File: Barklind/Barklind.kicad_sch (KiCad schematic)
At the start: 4 parts, among them J1 Molex 47053-1000, J2 Molex 47053-1000, J3 Molex 47053-1000, J4 RJ45_Abracon_ARJP11A-MASA-B-A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

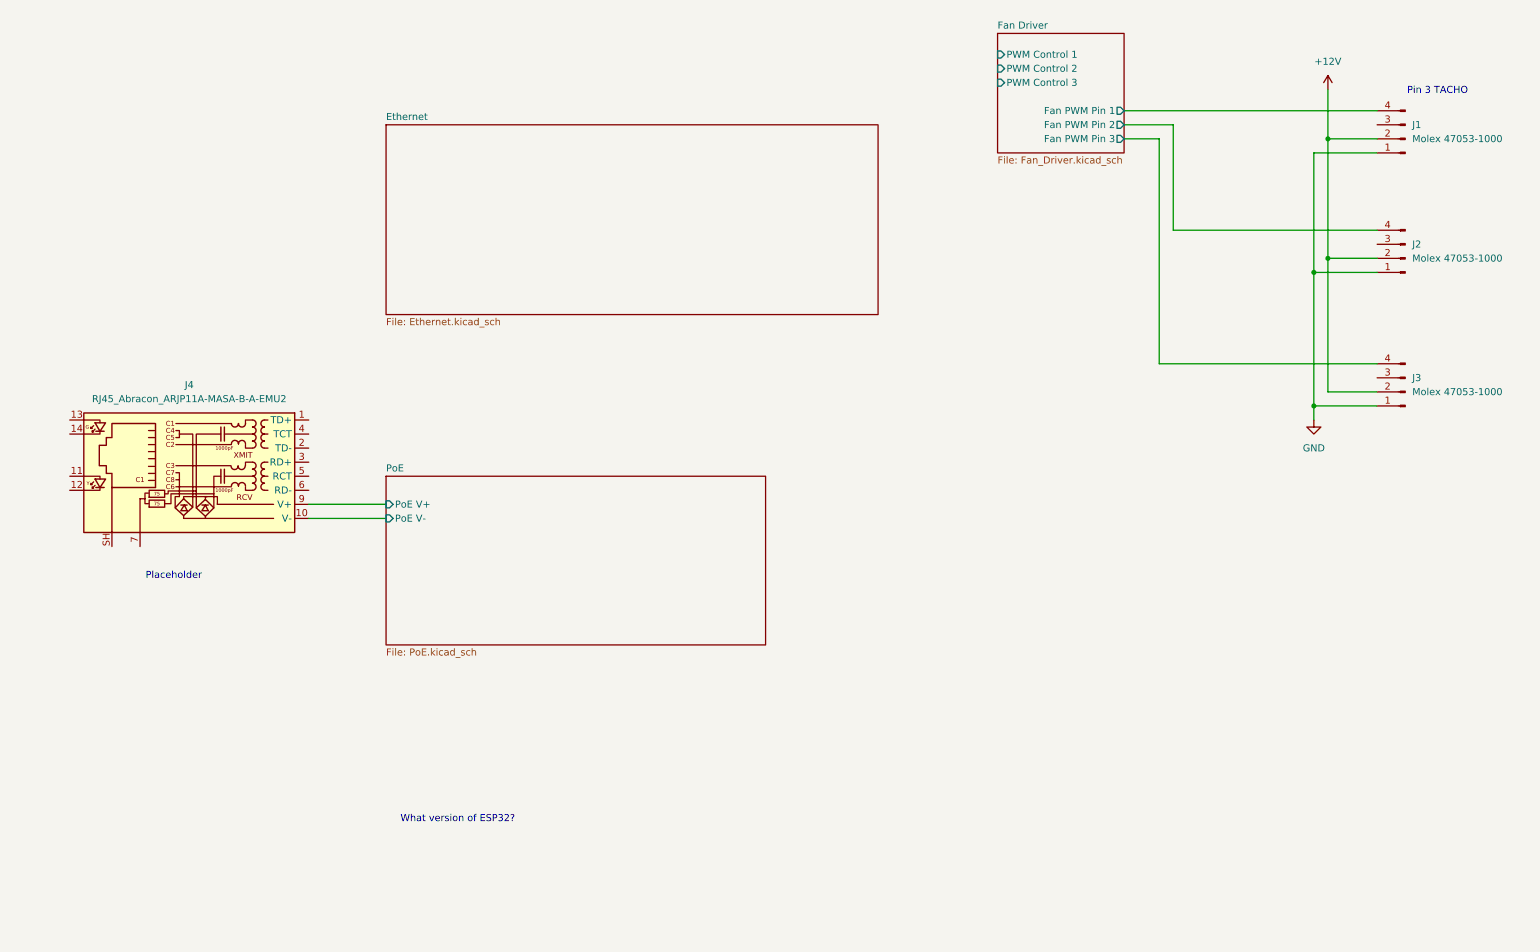
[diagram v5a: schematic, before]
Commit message: Added ESP32-DevkitC Updated workflow to commit changes (adding built docs) Removed manually exported PDF schematic in favour of auto-exported schematic
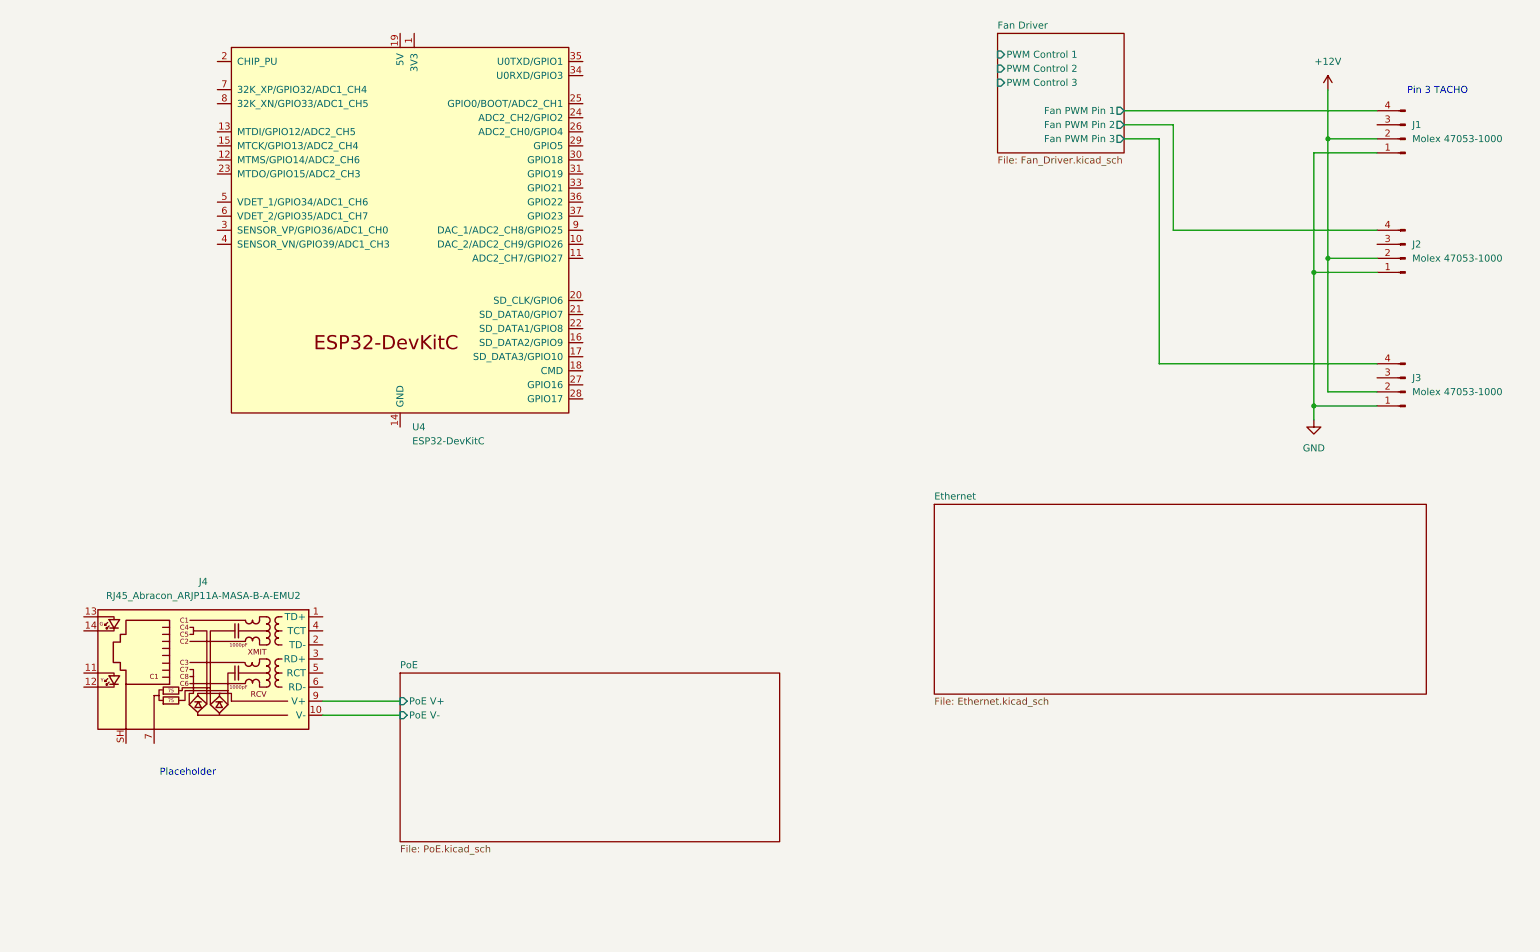
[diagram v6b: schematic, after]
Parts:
- added U4: ESP32-DevKitC, PCM_Espressif:ESP32-DevKitC, symbol ESP32-Symbols:ESP32-DevKitC
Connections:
- new net: U4.14 (GND), U4.32 (GND), U4.38 (GND)
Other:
- note removed: "What version of ESP32?"
- moved on the sheet: J4
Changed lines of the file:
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@@
 	(wire
 		(pts
-			(xy 66.04 116.84) (xy 80.01 116.84)
+			(xy 68.58 152.4) (xy 82.55 152.4)
 		)
 		(stroke
@@
 	(wire
 		(pts
-			(xy 66.04 114.3) (xy 80.01 114.3)
+			(xy 68.58 149.86) (xy 82.55 149.86)
 		)
 		(stroke
@@
 	(wire
 		(pts
-			(xy 219.71 88.9) (xy 219.71 48.26)
-		)
-		(stroke
-			(width 0)
-			(type default)
-		)
-	)
-	(wire
-		(pts
 			(xy 259.08 48.26) (xy 250.19 48.26)
 		)
@@
 	(wire
 		(pts
+			(xy 219.71 48.26) (xy 219.71 88.9)
+		)
+		(stroke
+			(width 0)
+			(type default)
+		)
+	)
+	(wire
+		(pts
 			(xy 219.71 48.26) (xy 213.36 48.26)
 		)
@@
 			(width 0)
 			(type default)
-		)
-	)
-	(text "What version of ESP32?"
-		(exclude_from_sim no)
-		(at 92.964 171.196 0)
-		(effects
-			(font
-				(size 1.27 1.27)
-			)
 		)
 	)
 	(text "Placeholder"
 		(exclude_from_sim no)
-		(at 41.656 127.254 0)
+		(at 44.196 162.814 0)
 		(effects
 			(font
@@
 	)
 	(symbol
+		(lib_id "ESP32-Symbols:ESP32-DevKitC")
+		(at 82.55 64.77 0)
+		(unit 1)
+		(exclude_from_sim no)
+		(in_bom yes)
+		(on_board yes)
+		(dnp no)
+		(fields_autoplaced yes)
+		(property "Reference" "U4"
+			(at 84.7441 100.33 0)
+			(effects
+				(font
+					(size 1.27 1.27)
+				)
+				(justify left)
+			)
+		)
+		(property "Value" "ESP32-DevKitC"
+			(at 84.7441 102.87 0)
+			(effects
+				(font
+					(size 1.27 1.27)
+				)
+				(justify left)
+			)
+		)
+		(property "Footprint" "PCM_Espressif:ESP32-DevKitC"
+			(at 82.55 107.95 0)
+			(effects
+				(font
+					(size 1.27 1.27)
+				)
+				(hide yes)
+			)
+		)
+		(property "Datasheet" "https://docs.espressif.com/projects/esp-idf/zh_CN/latest/esp32/hw-reference/esp32/get-started-devkitc.html"
+			(at 82.55 110.49 0)
+			(effects
+				(font
+					(size 1.27 1.27)
+				)
+				(hide yes)
+			)
+		)
+		(property "Description" "Development Kit"
+			(at 82.55 64.77 0)
+			(effects
+				(font
+					(size 1.27 1.27)
+				)
+				(hide yes)
+			)
+		)
+		(pin "11"
+		)
+		(pin "18"
+		)
+		(pin "3"
+		)
+		(pin "33"
+		)
+		(pin "5"
+		)
+		(pin "17"
+		)
+		(pin "6"
+		)
+		(pin "31"
+		)
+		(pin "25"
+		)
+		(pin "15"
+		)
+		(pin "1"
+		)
+		(pin "28"
+		)
+		(pin "22"
+		)
+		(pin "19"
+		)
+		(pin "2"
+		)
+		(pin "20"
+		)
+		(pin "24"
+		)
+		(pin "26"
+		)
+		(pin "32"
+		)
+		(pin "13"
+		)
+		(pin "35"
+		)
+		(pin "36"
+		)
+		(pin "37"
+		)
+		(pin "38"
+		)
+		(pin "7"
+		)
+		(pin "12"
+		)
+		(pin "30"
+		)
+		(pin "14"
+		)
+		(pin "4"
+		)
+		(pin "16"
+		)
+		(pin "34"
+		)
+		(pin "23"
+		)
+		(pin "10"
+		)
+		(pin "9"
+		)
+		(pin "8"
+		)
+		(pin "21"
+		)
+		(pin "27"
+		)
+		(pin "29"
+		)
+		(instances
+			(project ""
+				(path "/489e2a6e-50ed-4353-8289-8893922fad24"
+					(reference "U4")
+					(unit 1)
+				)
+			)
+		)
+	)
+	(symbol
 		(lib_id "Connector:Conn_01x04_Pin")
 		(at 264.16 69.85 180)
@@
 	(symbol
 		(lib_id "Connector:RJ45_Abracon_ARJP11A-MASA-B-A-EMU2")
-		(at 45.72 109.22 0)
+		(at 48.26 144.78 0)
 		(mirror y)
 		(unit 1)
@@
 		(dnp no)
 		(property "Reference" "J4"
-			(at 44.45 92.71 0)
+			(at 46.99 128.27 0)
 			(effects
 				(font
@@
 		)
 		(property "Value" "RJ45_Abracon_ARJP11A-MASA-B-A-EMU2"
-			(at 44.45 95.25 0)
+			(at 46.99 130.81 0)
 			(effects
 				(font
@@
 		)
 		(property "Footprint" "Connector_RJ:RJ45_Abracon_ARJP11A-MA_Horizontal"
-			(at 45.72 93.98 0)
+			(at 48.26 129.54 0)
 			(effects
 				(font
@@
 		)
 		(property "Datasheet" "https://abracon.com/Magnetics/lan/ARJP11A.PDF"
-			(at 45.72 91.44 0)
+			(at 48.26 127 0)
 			(effects
 				(font
@@
 		)
 		(property "Description" "RJ45 PoE 10/100 Base-TX Jack with Magnetic Module"
-			(at 45.72 109.22 0)
+			(at 48.26 144.78 0)
 			(effects
 				(font
@@
 	)
 	(sheet
-		(at 80.01 45.72)
+		(at 179.07 114.3)
 		(size 88.9 34.29)
 		(fields_autoplaced yes)
@@
 		)
 		(property "Sheetname" "Ethernet"
-			(at 80.01 45.0084 0)
+			(at 179.07 113.5884 0)
 			(effects
 				(font
@@
 		)
 		(property "Sheetfile" "Ethernet.kicad_sch"
-			(at 80.01 80.5946 0)
+			(at 179.07 149.1746 0)
 			(effects
 				(font
@@
 	)
 	(sheet
-		(at 80.01 109.22)
+		(at 82.55 144.78)
 		(size 68.58 30.48)
 		(fields_autoplaced yes)
@@
 		)
 		(property "Sheetname" "PoE"
-			(at 80.01 108.5084 0)
+			(at 82.55 144.0684 0)
 			(effects
 				(font
@@
 		)
 		(property "Sheetfile" "PoE.kicad_sch"
-			(at 80.01 140.2846 0)
+			(at 82.55 175.8446 0)
 			(effects
 				(font
@@
 		)
 		(pin "PoE V+" input
-			(at 80.01 114.3 180)
+			(at 82.55 149.86 180)
 			(effects
 				(font
@@
 		)
 		(pin "PoE V-" input
-			(at 80.01 116.84 180)
-			(effects
-				(font
+			(at 82.55 152.4 180)
+			(effects
+				(font

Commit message: Added most components to Ethernet schematic Updated main schematic to add connections to/from ethernet schematic Added connections from ESP32 to Fan driver
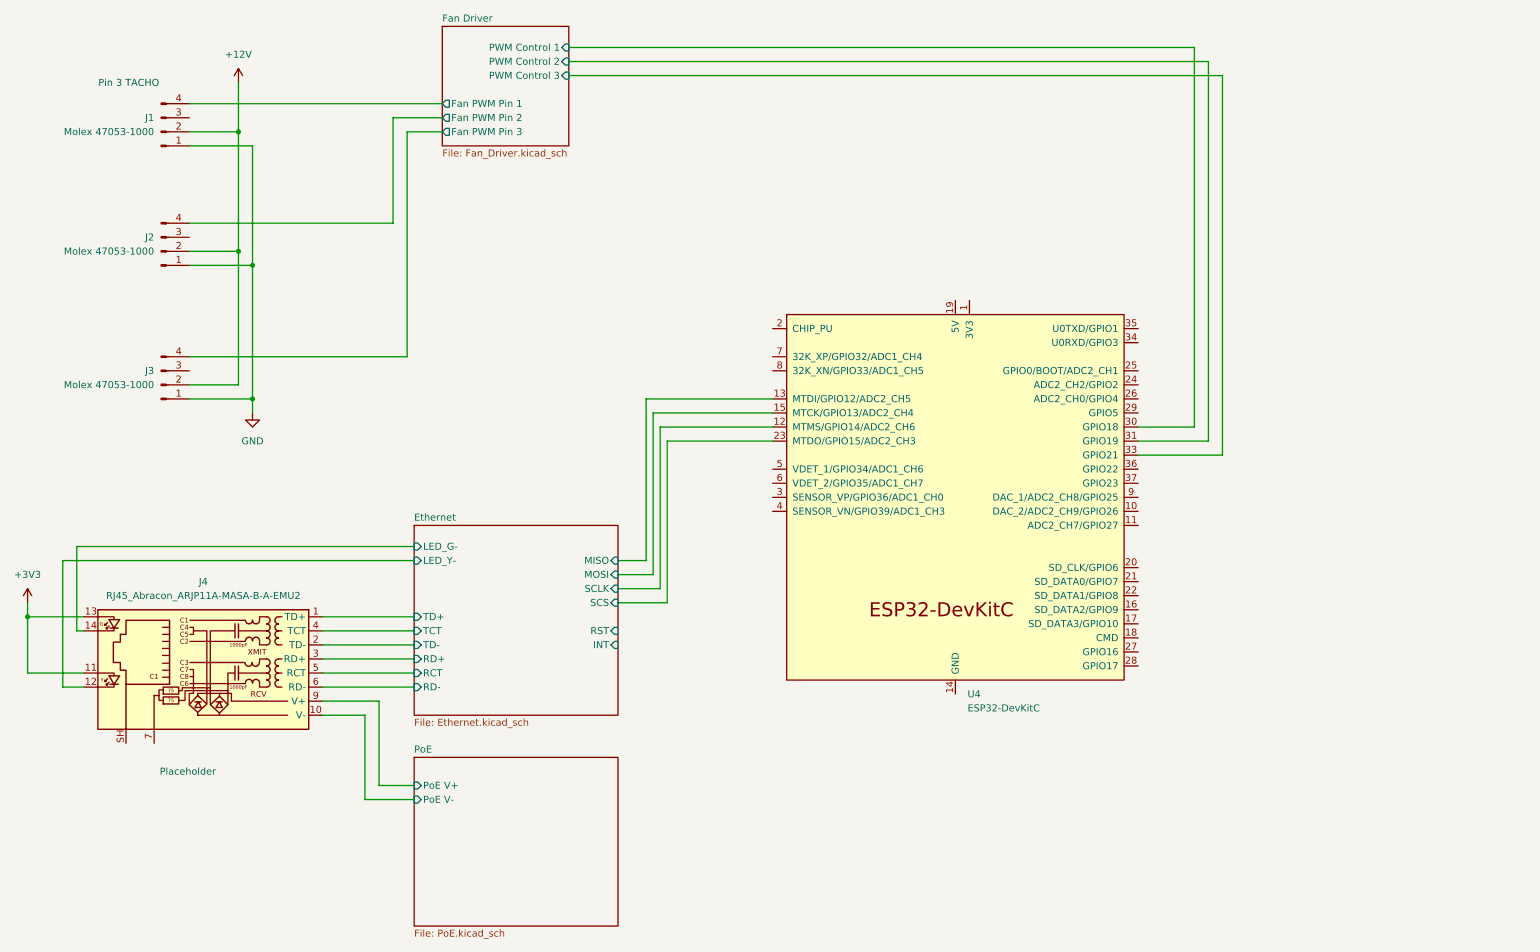
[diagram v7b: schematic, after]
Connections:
- net Fan Driver/PWM Control 1: now also U4.30 (GPIO18)
- net Fan Driver/PWM Control 2: now also U4.31 (GPIO19)
- net Fan Driver/PWM Control 3: now also U4.33 (GPIO21)
- net Ethernet/SCLK: now reaches U4.12 (MTMS/GPIO14/ADC2_CH6)
- net Ethernet/MISO: now reaches U4.13 (MTDI/GPIO12/ADC2_CH5)
- net Ethernet/MOSI: now reaches U4.15 (MTCK/GPIO13/ADC2_CH4)
- net Ethernet/SCS: now reaches U4.23 (MTDO/GPIO15/ADC2_CH3)
- net Ethernet/TD+: now reaches J4.1 (TD+)
- net +3V3: now reaches J4.11
- net +3V3: now also J4.13
- net Ethernet/LED_Y-: now reaches J4.12
- net Ethernet/LED_G-: now reaches J4.14
- net Ethernet/TD-: now reaches J4.2 (TD-)
- net Ethernet/RD+: now reaches J4.3 (RD+)
- net Ethernet/TCT: now reaches J4.4 (TCT)
- net Ethernet/RCT: now reaches J4.5 (RCT)
- net Ethernet/RD-: now reaches J4.6 (RD-)
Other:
- sheet Ethernet ports: added INT, LED_G-, LED_Y-, MISO, MOSI, RCT, RD+, RD-, RST, SCLK, SCS, TCT, TD+, TD-; removed none
- moved on the sheet: J1, J2, J3, U4

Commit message: Added and connected ESP32-Pin-Headers
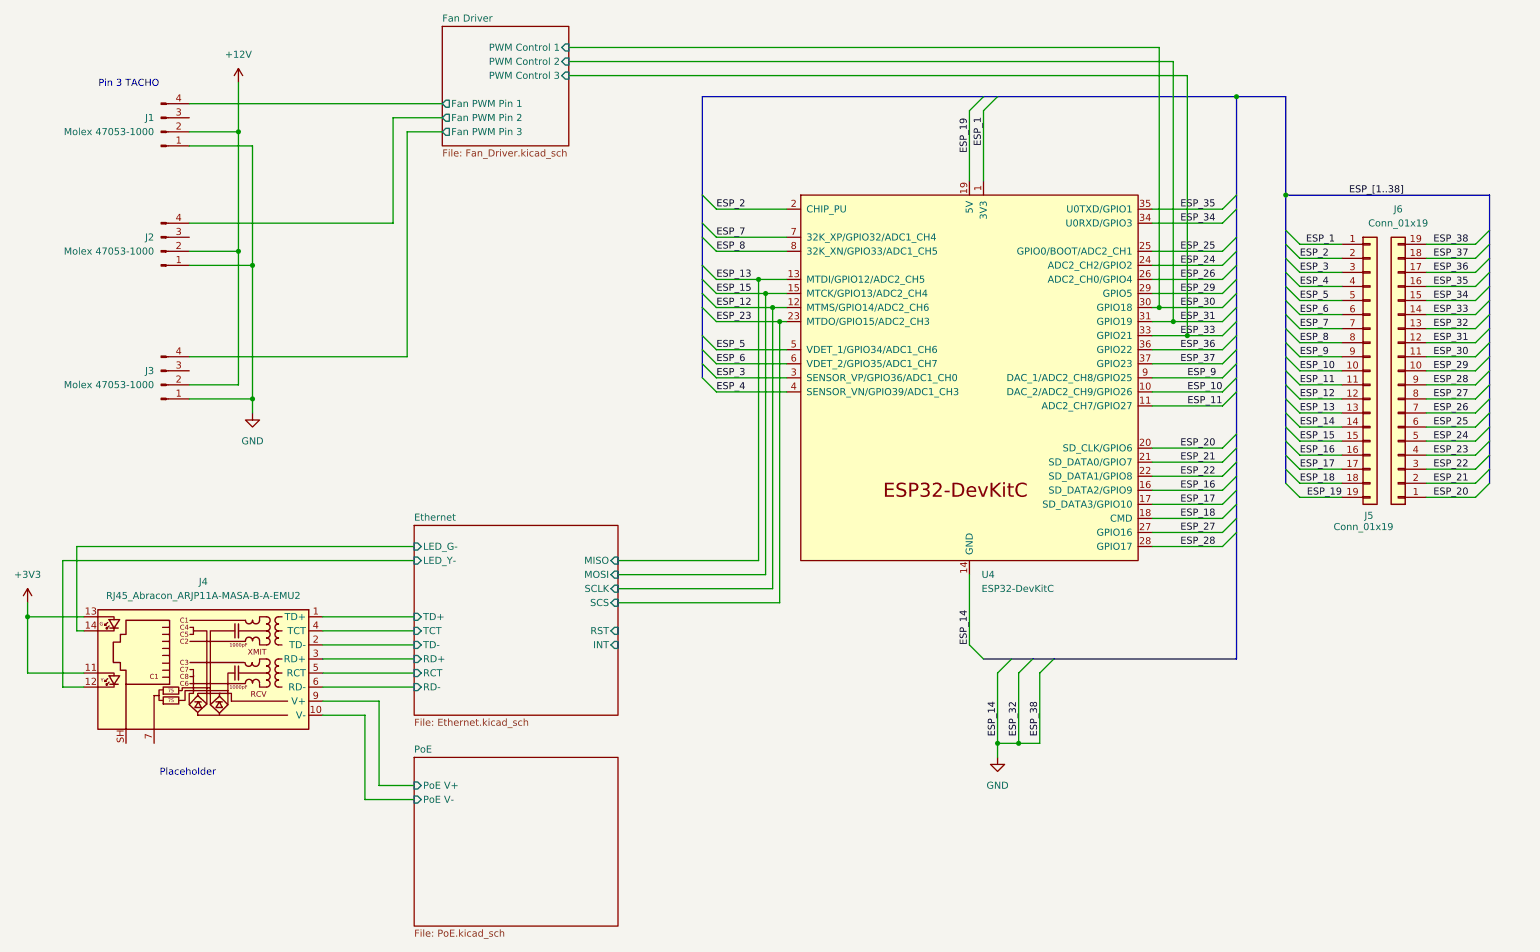
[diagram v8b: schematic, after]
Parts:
- added J5, J6: Conn_01x19, symbol Connector_Generic:Conn_01x19
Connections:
- net GND: now also U4.14 (GND), U4.32 (GND), U4.38 (GND), J5.14 (Pin_14), J6.13 (Pin_13), J6.19 (Pin_19)
- net ESP_1: now reaches U4.1 (3V3)
- net ESP_1: now also J5.1 (Pin_1)
- net ESP_10: now reaches U4.10 (DAC_2/ADC2_CH9/GPIO26)
- net ESP_10: now also J5.10 (Pin_10)
- net ESP_11: now reaches U4.11 (ADC2_CH7/GPIO27)
- net ESP_11: now also J5.11 (Pin_11)
- net ESP_16: now reaches U4.16 (SD_DATA2/GPIO9)
- net ESP_16: now also J5.16 (Pin_16)
- net ESP_17: now reaches U4.17 (SD_DATA3/GPIO10)
- net ESP_17: now also J5.17 (Pin_17)
- net ESP_18: now reaches U4.18 (CMD)
- net ESP_18: now also J5.18 (Pin_18)
- net ESP_19: now reaches U4.19 (5V)
- net ESP_19: now also J5.19 (Pin_19)
- net ESP_2: now reaches U4.2 (CHIP_PU)
- net ESP_2: now also J5.2 (Pin_2)
- net ESP_20: now reaches U4.20 (SD_CLK/GPIO6)
- net ESP_20: now also J6.1 (Pin_1)
- net ESP_21: now reaches U4.21 (SD_DATA0/GPIO7)
- net ESP_21: now also J6.2 (Pin_2)
- net ESP_22: now reaches U4.22 (SD_DATA1/GPIO8)
- net ESP_22: now also J6.3 (Pin_3)
- net ESP_24: now reaches U4.24 (ADC2_CH2/GPIO2)
- net ESP_24: now also J6.5 (Pin_5)
- net ESP_25: now reaches U4.25 (GPIO0/BOOT/ADC2_CH1)
- net ESP_25: now also J6.6 (Pin_6)
- net ESP_26: now reaches U4.26 (ADC2_CH0/GPIO4)
- net ESP_26: now also J6.7 (Pin_7)
- net ESP_27: now reaches U4.27 (GPIO16)
- net ESP_27: now also J6.8 (Pin_8)
- net ESP_28: now reaches U4.28 (GPIO17)
- net ESP_28: now also J6.9 (Pin_9)
- net ESP_29: now reaches U4.29 (GPIO5)
- net ESP_29: now also J6.10 (Pin_10)
- net ESP_3: now reaches U4.3 (SENSOR_VP/GPIO36/ADC1_CH0)
- net ESP_3: now also J5.3 (Pin_3)
- net ESP_34: now reaches U4.34 (U0RXD/GPIO3)
- net ESP_34: now also J6.15 (Pin_15)
- net ESP_35: now reaches U4.35 (U0TXD/GPIO1)
- net ESP_35: now also J6.16 (Pin_16)
- net ESP_36: now reaches U4.36 (GPIO22)
- net ESP_36: now also J6.17 (Pin_17)
- net ESP_37: now reaches U4.37 (GPIO23)
- net ESP_37: now also J6.18 (Pin_18)
- net ESP_4: now reaches U4.4 (SENSOR_VN/GPIO39/ADC1_CH3)
- net ESP_4: now also J5.4 (Pin_4)
- net ESP_5: now reaches U4.5 (VDET_1/GPIO34/ADC1_CH6)
- net ESP_5: now also J5.5 (Pin_5)
- net ESP_6: now reaches U4.6 (VDET_2/GPIO35/ADC1_CH7)
- net ESP_6: now also J5.6 (Pin_6)
- net ESP_7: now reaches U4.7 (32K_XP/GPIO32/ADC1_CH4)
- net ESP_7: now also J5.7 (Pin_7)
- net ESP_8: now reaches U4.8 (32K_XN/GPIO33/ADC1_CH5)
- net ESP_8: now also J5.8 (Pin_8)
- net ESP_9: now reaches U4.9 (DAC_1/ADC2_CH8/GPIO25)
- net ESP_9: now also J5.9 (Pin_9)
- net Ethernet/MISO renamed ESP_13
- net ESP_13: now also J5.13 (Pin_13)
- net Ethernet/MOSI renamed ESP_15
- net ESP_15: now also J5.15 (Pin_15)
- net Ethernet/SCLK renamed ESP_12
- net ESP_12: now also J5.12 (Pin_12)
- net Ethernet/SCS renamed ESP_23
- net ESP_23: now also J6.4 (Pin_4)
- net Fan Driver/PWM Control 1 renamed ESP_30
- net ESP_30: now also J6.11 (Pin_11)
- net Fan Driver/PWM Control 2 renamed ESP_31
- net ESP_31: now also J6.12 (Pin_12)
- net Fan Driver/PWM Control 3 renamed ESP_33
- net ESP_33: now also J6.14 (Pin_14)
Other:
- moved on the sheet: U4
